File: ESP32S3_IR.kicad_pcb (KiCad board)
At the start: 2 copper layers, 18 x 53.5 mm, 11 parts, among them J1 ESP32_Right, J2 ESP32_Left, J3 I2C, SW1 C318938, SW2 C318938, SW3 C318938

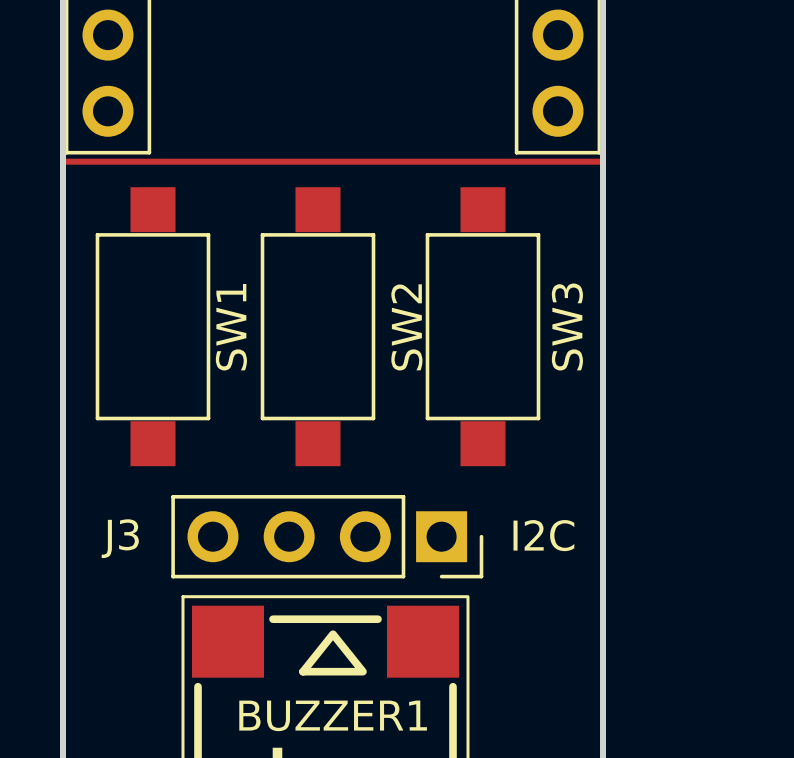
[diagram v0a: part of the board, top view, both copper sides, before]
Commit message: update layout: change OLED placement
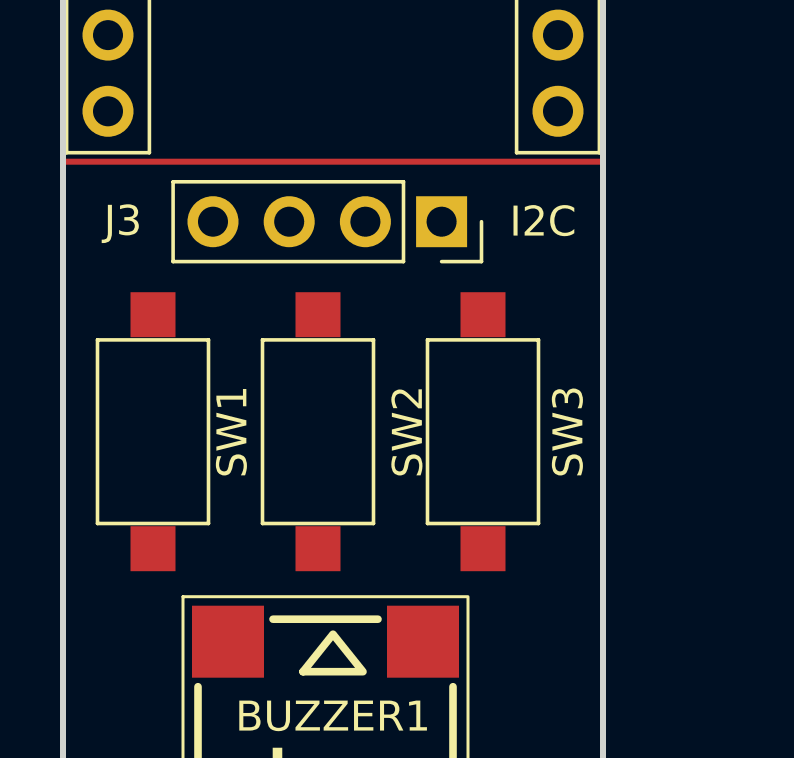
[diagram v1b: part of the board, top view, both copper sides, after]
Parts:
- moved J3 10.5 mm to (162.6, 81.5)
- moved SW1 3.50 mm to (153.0, 88.5)
- moved SW2 3.50 mm to (158.5, 88.5)
- moved SW3 3.50 mm to (164.0, 88.5)
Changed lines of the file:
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@@
 	(footprint "Connector_PinSocket_2.54mm:PinSocket_1x04_P2.54mm_Vertical"
 		(layer "F.Cu")
-		(at 162.62 92 -90)
+		(at 162.62 81.5 -90)
 		(descr "Through hole straight socket strip, 1x04, 2.54mm pitch, single row (from Kicad 4.0.7), script generated")
 		(tags "Through hole socket strip THT 1x04 2.54mm single row")
@@
 	(footprint "Button_Switch_SMD:SW_SPST_CK_RS282G05A3"
 		(layer "F.Cu")
-		(at 164 85 90)
+		(at 164 88.5 90)
 		(descr "https://www.mouser.com/ds/2/60/RS-282G05A-SM_RT-1159762.pdf")
 		(tags "SPST button tactile switch")
@@
 	(footprint "Button_Switch_SMD:SW_SPST_CK_RS282G05A3"
 		(layer "F.Cu")
-		(at 153 85 90)
+		(at 153 88.5 90)
 		(descr "https://www.mouser.com/ds/2/60/RS-282G05A-SM_RT-1159762.pdf")
 		(tags "SPST button tactile switch")
@@
 	(footprint "Button_Switch_SMD:SW_SPST_CK_RS282G05A3"
 		(layer "F.Cu")
-		(at 158.5 85 90)
+		(at 158.5 88.5 90)
 		(descr "https://www.mouser.com/ds/2/60/RS-282G05A-SM_RT-1159762.pdf")
 		(tags "SPST button tactile switch")

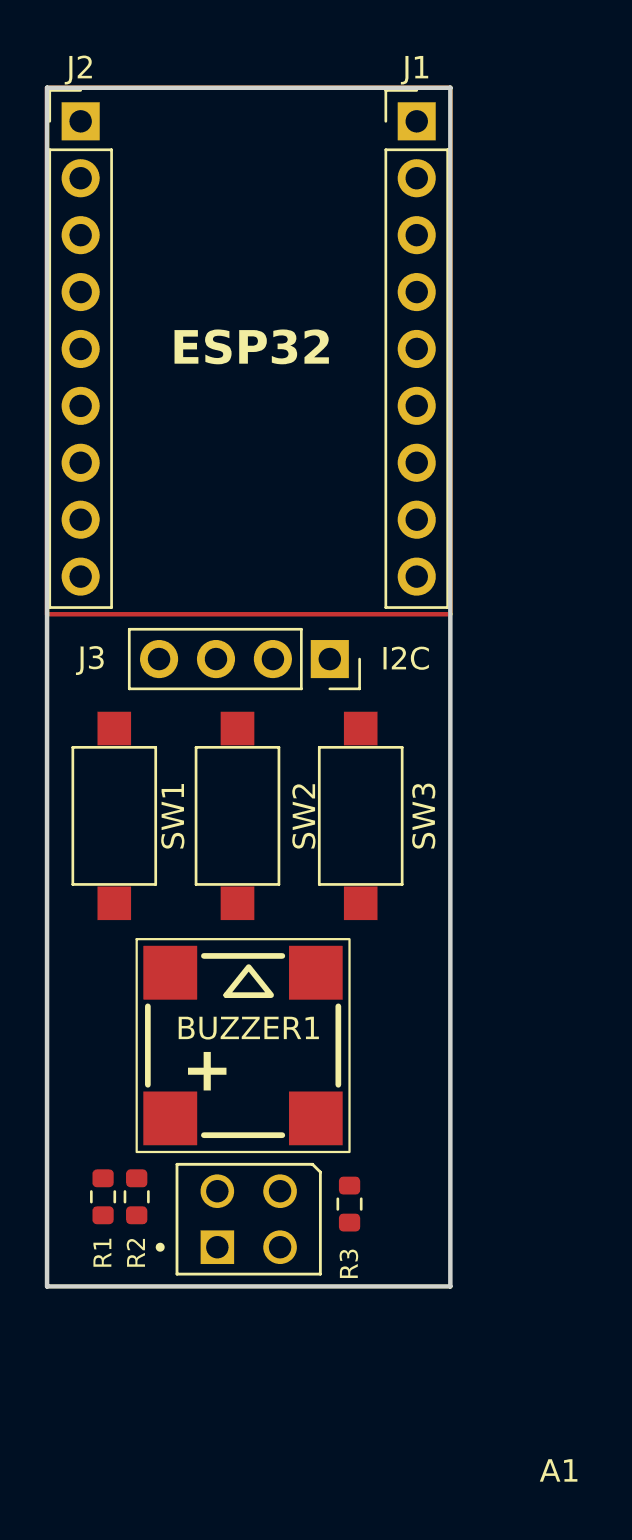
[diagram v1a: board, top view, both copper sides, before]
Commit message: Flip all except ESP32 -> B.Cu
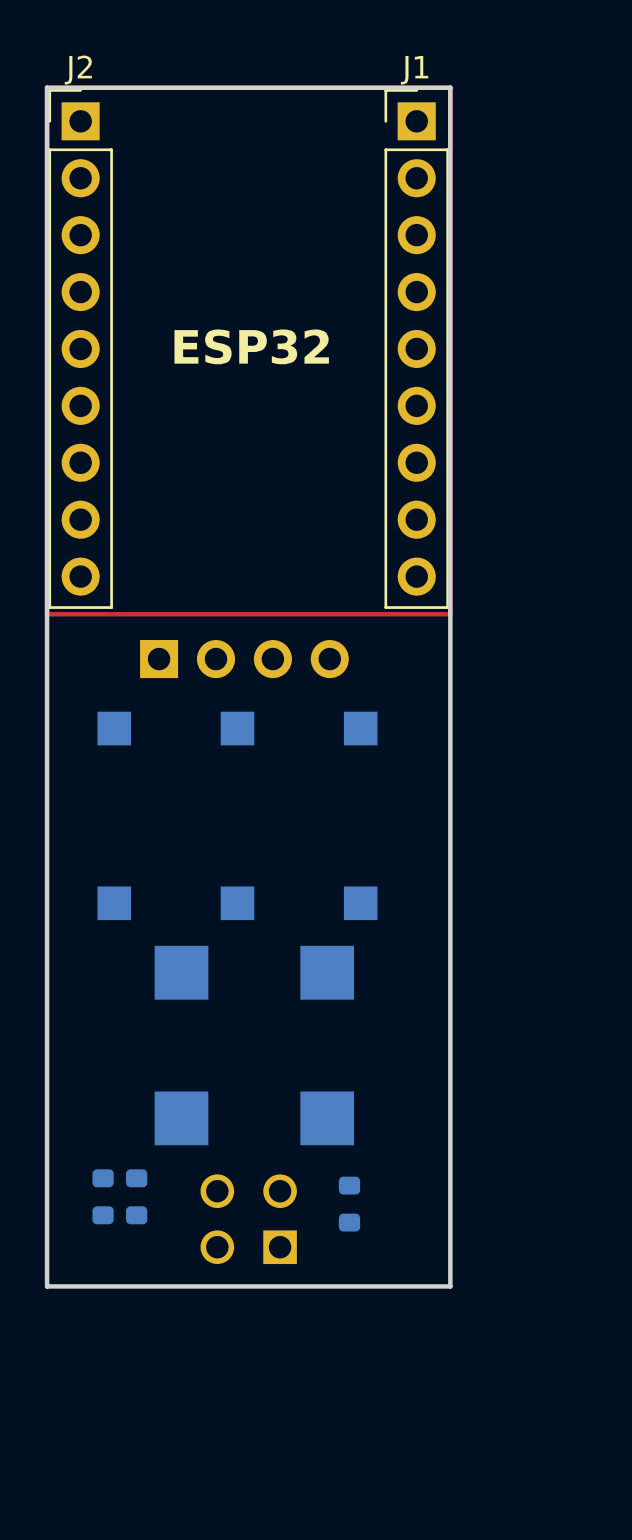
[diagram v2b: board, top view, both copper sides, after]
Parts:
- A1, BUZZER1, J3, R1, R2, R3, SW1, SW2, SW3: moved to B.Cu
- moved J3 7.62 mm to (155.0, 81.5)
- turned A1 to 180 degrees
- turned BUZZER1 to 180 degrees

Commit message: update SCH: add battery sensor ADC  & split net into 3V3 & 5V powerline.
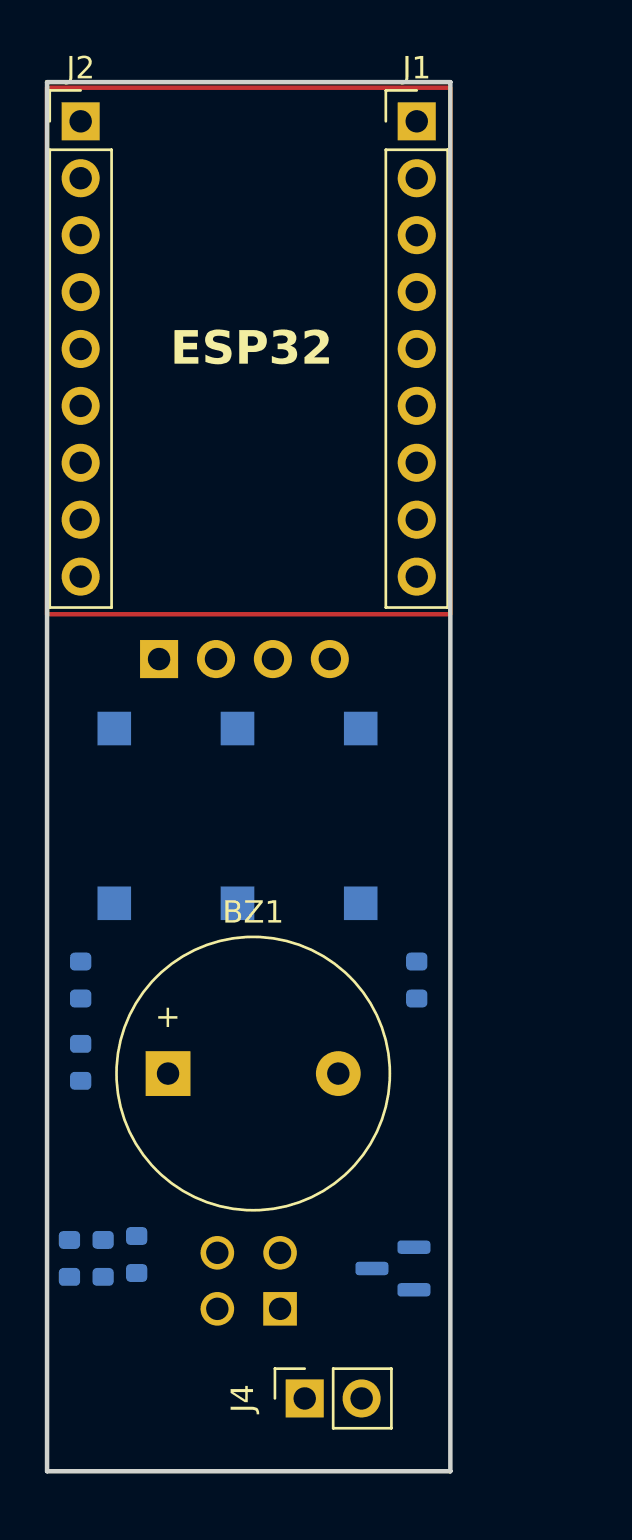
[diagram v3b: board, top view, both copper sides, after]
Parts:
- removed BUZZER1: C94599, Buzzer_Beeper:MLT-8530
- added BZ1: Buzzer, Buzzer_Beeper:Buzzer_12x9.5RM7.6, F.Cu at (155.4, 100.0)
- added J4: PWR, Connector_PinSocket_2.54mm:PinSocket_1x02_P2.54mm_Vertical, F.Cu at (161.5, 114.5)
- added Q1: MMBT2222A, Package_TO_SOT_SMD:SOT-23, B.Cu at (165.4, 108.7)
- added R4: 1K, Resistor_SMD:R_0603_1608Metric, B.Cu at (166.5, 95.8)
- added R5: 68K, Resistor_SMD:R_0603_1608Metric, B.Cu at (151.5, 95.8)
- added R6: 100K, Resistor_SMD:R_0603_1608Metric, B.Cu at (151.5, 99.5)
- moved R3 9.76 mm to (154.0, 108.1)
- moved R1 3.13 mm to (151.0, 108.2)
- moved R2 3.13 mm to (152.5, 108.2)
- moved A1 2.75 mm to (159.0, 109.2)
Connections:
- net /GND renamed GND
- J1 pad 1: /VCC -> /5V
- J3 pad 3: /VCC -> /3V3
- R1 pad 2: /VCC -> /3V3
- R3 pad 1: /VCC -> /3V3
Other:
- board size 18 x 53.5 mm -> 18 x 62 mm

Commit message: change ADC sensor pin 3V3 -> BAT socket
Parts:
- added J5: BAT, Connector_PinSocket_2.54mm:PinSocket_1x01_P2.54mm_Vertical, F.Cu at (152.5, 114.5)
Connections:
- R5 pad 1: /3V3 -> Net-(J5-Pin_1)
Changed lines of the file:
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@@
 	(net 21 "/5V")
 	(net 22 "Net-(Q1-B)")
+	(net 23 "Net-(J5-Pin_1)")
+	(footprint "Connector_PinSocket_2.54mm:PinSocket_1x01_P2.54mm_Vertical"
+		(layer "F.Cu")
+		(at 152.5 114.5)
+		(descr "Through hole straight socket strip, 1x01, 2.54mm pitch, single row (from Kicad 4.0.7), script generated")
+		(tags "Through hole socket strip THT 1x01 2.54mm single row")
+		(property "Reference" "J5"
+			(at 0 -2.77 0)
+			(layer "F.SilkS")
+			(effects
+				(font
+					(size 1 1)
+					(thickness 0.15)
+				)
+			)
+		)
+		(property "Value" "BAT"
+			(at 0 2.77 0)
+			(layer "F.Fab")
+			(effects
+				(font
+					(size 1 1)
+					(thickness 0.15)
+				)
+			)
+		)
+		(property "Datasheet" ""
+			(at 0 0 0)
+			(layer "F.Fab")
+			(hide yes)
+			(effects
+				(font
+					(size 1.27 1.27)
+					(thickness 0.15)
+				)
+			)
+		)
+		(property "Description" "Generic connector, single row, 01x01, script generated"
+			(at 0 0 0)
+			(layer "F.Fab")
+			(hide yes)
+			(effects
+				(font
+					(size 1.27 1.27)
+					(thickness 0.15)
+				)
+			)
+		)
+		(property ki_fp_filters "Connector*:*_1x??_*")
+		(sheetname "/")
+		(sheetfile "ESP32S3_IR.kicad_sch")
+		(attr through_hole)
+		(fp_line
+			(start -1.33 1.21)
+			(end -1.33 1.33)
+			(stroke
+				(width 0.12)
+				(type solid)
+			)
+			(layer "F.SilkS")
+		)
+		(fp_line
+			(start -1.33 1.33)
+			(end 1.33 1.33)
+			(stroke
+				(width 0.12)
+				(type solid)
+			)
+			(layer "F.SilkS")
+		)
+		(fp_line
+			(start 0 -1.33)
+			(end 1.33 -1.33)
+			(stroke
+				(width 0.12)
+				(type solid)
+			)
+			(layer "F.SilkS")
+		)
+		(fp_line
+			(start 1.33 -1.33)
+			(end 1.33 0)
+			(stroke
+				(width 0.12)
+				(type solid)
+			)
+			(layer "F.SilkS")
+		)
+		(fp_line
+			(start 1.33 1.21)
+			(end 1.33 1.33)
+			(stroke
+				(width 0.12)
+				(type solid)
+			)
+			(layer "F.SilkS")
+		)
+		(fp_line
+			(start -1.8 -1.8)
+			(end 1.75 -1.8)
+			(stroke
+				(width 0.05)
+				(type solid)
+			)
+			(layer "F.CrtYd")
+		)
+		(fp_line
+			(start -1.8 1.75)
+			(end -1.8 -1.8)
+			(stroke
+				(width 0.05)
+				(type solid)
+			)
+			(layer "F.CrtYd")
+		)
+		(fp_line
+			(start 1.75 -1.8)
+			(end 1.75 1.75)
+			(stroke
+				(width 0.05)
+				(type solid)
+			)
+			(layer "F.CrtYd")
+		)
+		(fp_line
+			(start 1.75 1.75)
+			(end -1.8 1.75)
+			(stroke
+				(width 0.05)
+				(type solid)
+			)
+			(layer "F.CrtYd")
+		)
+		(fp_line
+			(start -1.27 -1.27)
+			(end 0.635 -1.27)
+			(stroke
+				(width 0.1)
+				(type solid)
+			)
+			(layer "F.Fab")
+		)
+		(fp_line
+			(start -1.27 1.27)
+			(end -1.27 -1.27)
+			(stroke
+				(width 0.1)
+				(type solid)
+			)
+			(layer "F.Fab")
+		)
+		(fp_line
+			(start 0.635 -1.27)
+			(end 1.27 -0.635)
+			(stroke
+				(width 0.1)
+				(type solid)
+			)
+			(layer "F.Fab")
+		)
+		(fp_line
+			(start 1.27 -0.635)
+			(end 1.27 1.27)
+			(stroke
+				(width 0.1)
+				(type solid)
+			)
+			(layer "F.Fab")
+		)
+		(fp_line
+			(start 1.27 1.27)
+			(end -1.27 1.27)
+			(stroke
+				(width 0.1)
+				(type solid)
+			)
+			(layer "F.Fab")
+		)
+		(fp_text user "${REFERENCE}"
+			(at 0 0 0)
+			(layer "F.Fab")
+			(effects
+				(font
+					(size 1 1)
+					(thickness 0.15)
+				)
+			)
+		)
+		(pad "1" thru_hole rect
+			(at 0 0)
+			(size 1.7 1.7)
+			(drill 1)
+			(layers "*.Cu" "*.Mask")
+			(remove_unused_layers no)
+			(net 23 "Net-(J5-Pin_1)")
+			(pinfunction "Pin_1")
+			(pintype "passive")
+		)
+		(embedded_fonts no)
+		(model "${KICAD9_3DMODEL_DIR}/Connector_PinSocket_2.54mm.3dshapes/PinSocket_1x01_P2.54mm_Vertical.wrl"
+			(offset
+				(xyz 0 0 0)
+			)
+			(scale
+				(xyz 1 1 1)
+			)
+			(rotate
+				(xyz 0 0 0)
+			)
+		)
+	)
 	(footprint "Connector_PinHeader_2.54mm:PinHeader_1x09_P2.54mm_Vertical"
 		(layer "F.Cu")
@@
 			(layers "B.Cu" "B.Mask" "B.Paste")
 			(roundrect_rratio 0.25)
-			(net 6 "/3V3")
-			(pintype "passive")
-		)
+			(net 23 "Net-(J5-Pin_1)")
+			(pintype "passive")
+		)

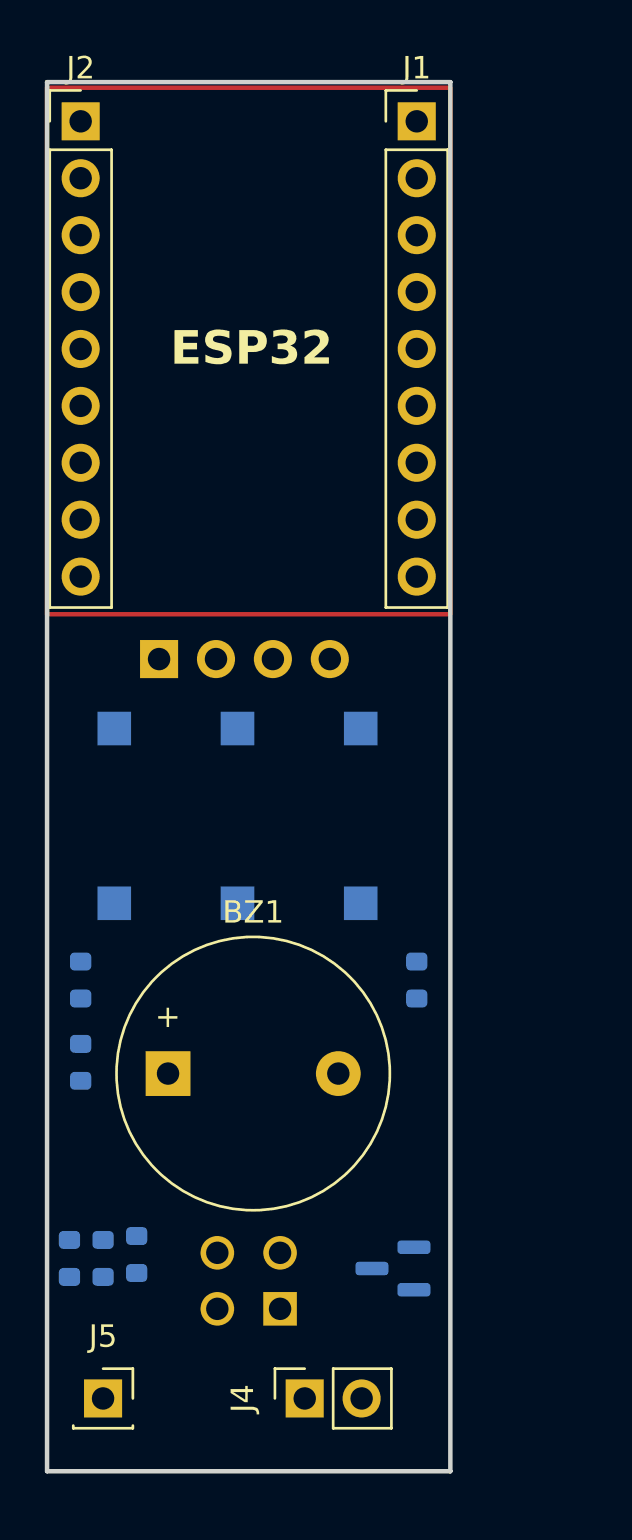
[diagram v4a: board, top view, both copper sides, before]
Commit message: Change Layout-> Fit Early THT requirement
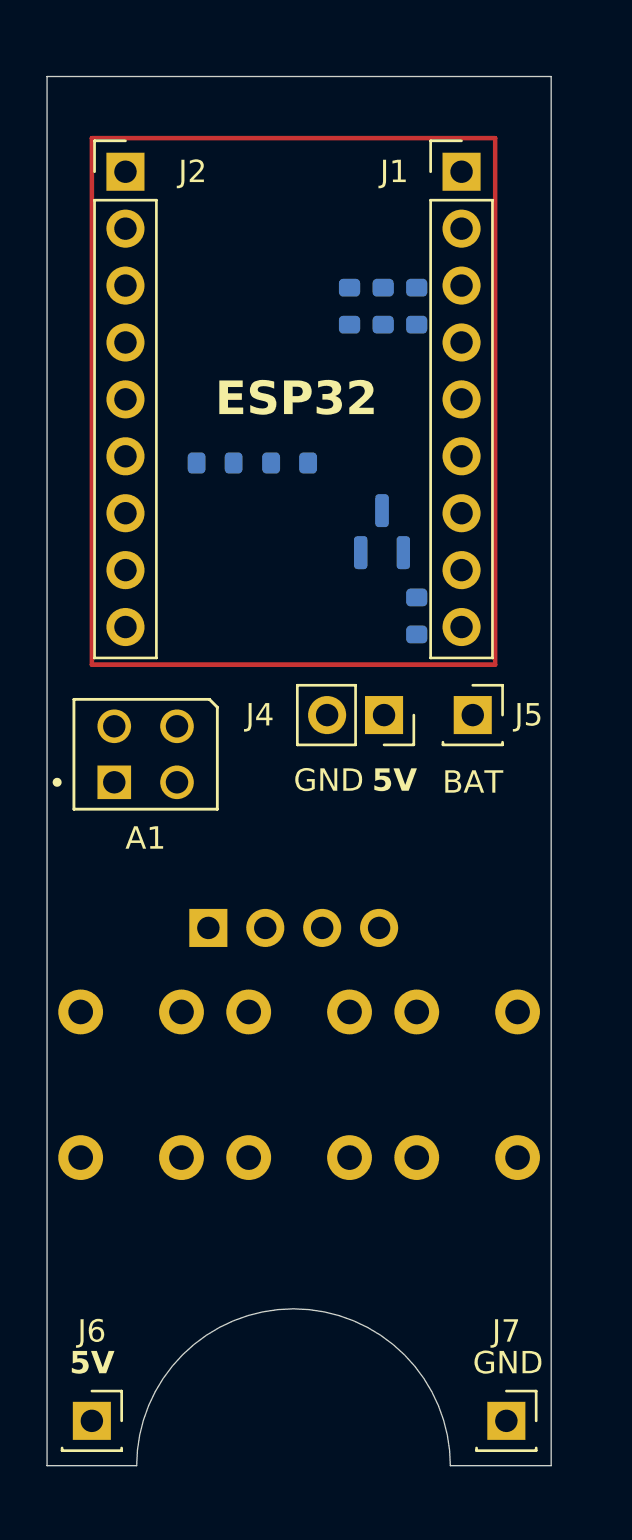
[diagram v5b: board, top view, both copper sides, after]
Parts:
- removed BZ1: Buzzer, Buzzer_Beeper:Buzzer_12x9.5RM7.6
- added J6: BUZZER_5V, Connector_PinSocket_2.54mm:PinSocket_1x01_P2.54mm_Vertical, F.Cu at (152.0, 115.5)
- added J7: BUZZER_GND, Connector_PinSocket_2.54mm:PinSocket_1x01_P2.54mm_Vertical, F.Cu at (170.5, 115.5)
- A1: moved to F.Cu
- SW1, SW2, SW3: footprint Button_Switch_SMD:SW_SPST_CK_RS282G05A3 -> Button_Switch_THT:SW_PUSH_6mm
- moved R1 44.7 mm to (165.0, 65.8)
- moved R2 44.7 mm to (166.5, 65.8)
- moved R3 43.4 mm to (163.5, 65.8)
- moved J5 34.7 mm to (169.0, 84.0)
- moved Q1 32.9 mm to (164.9, 75.8), turned to 90 degrees
- moved J4 30.7 mm to (165.0, 84.0), turned to -90 degrees
- moved R6 28.3 mm to (160.8, 72.8), turned to 0 degrees
- moved A1 23.9 mm to (154.4, 85.8), turned to 0 degrees
- moved R5 23.8 mm to (157.5, 72.8), turned to 180 degrees
- moved SW3 16.8 mm to (171.0, 103.8)
- moved R4 16.2 mm to (166.5, 79.6)
- moved SW2 16.0 mm to (163.5, 103.8)
- moved SW1 15.5 mm to (156.0, 103.8)
- moved J3 12.2 mm to (157.2, 93.5)
- moved J1 3.01 mm to (168.5, 59.8)
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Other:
- board size 18 x 62 mm -> 22.5 x 62 mm
- board text added: "22mm"
- board text added: "40mm"
- board text added: "5V"
- board text added: "GND"
- board text added: "GND VCC SCL SDA"
